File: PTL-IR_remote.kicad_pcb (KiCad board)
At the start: 2 copper layers, 25.4 x 40.1 mm, 22 parts, among them J1 8p, J2 8p, J3 bme280, J4 Conn_01x03_Female, Q1 2N7002, U1 TSOP4838

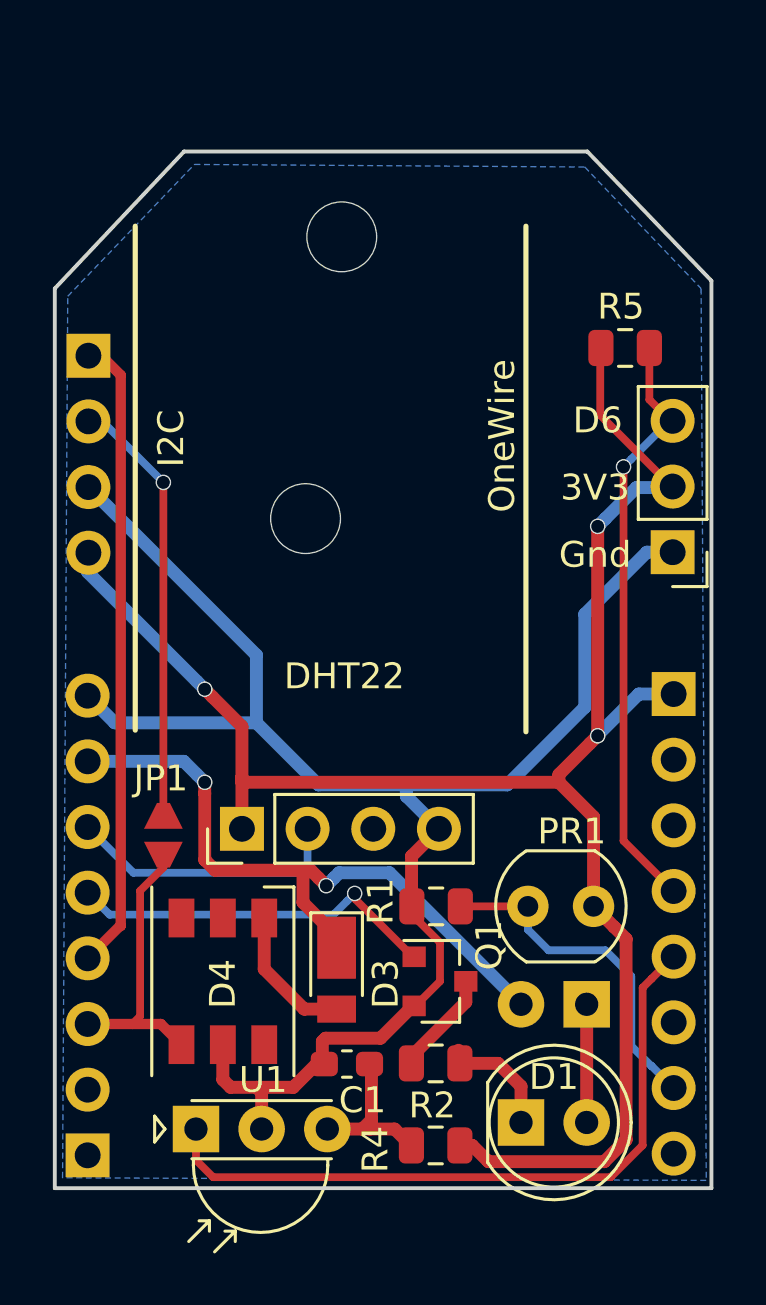
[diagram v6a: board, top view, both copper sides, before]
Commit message: Moved to Kicad5 Fixed swap of 5V and GND PCB is now V1.2
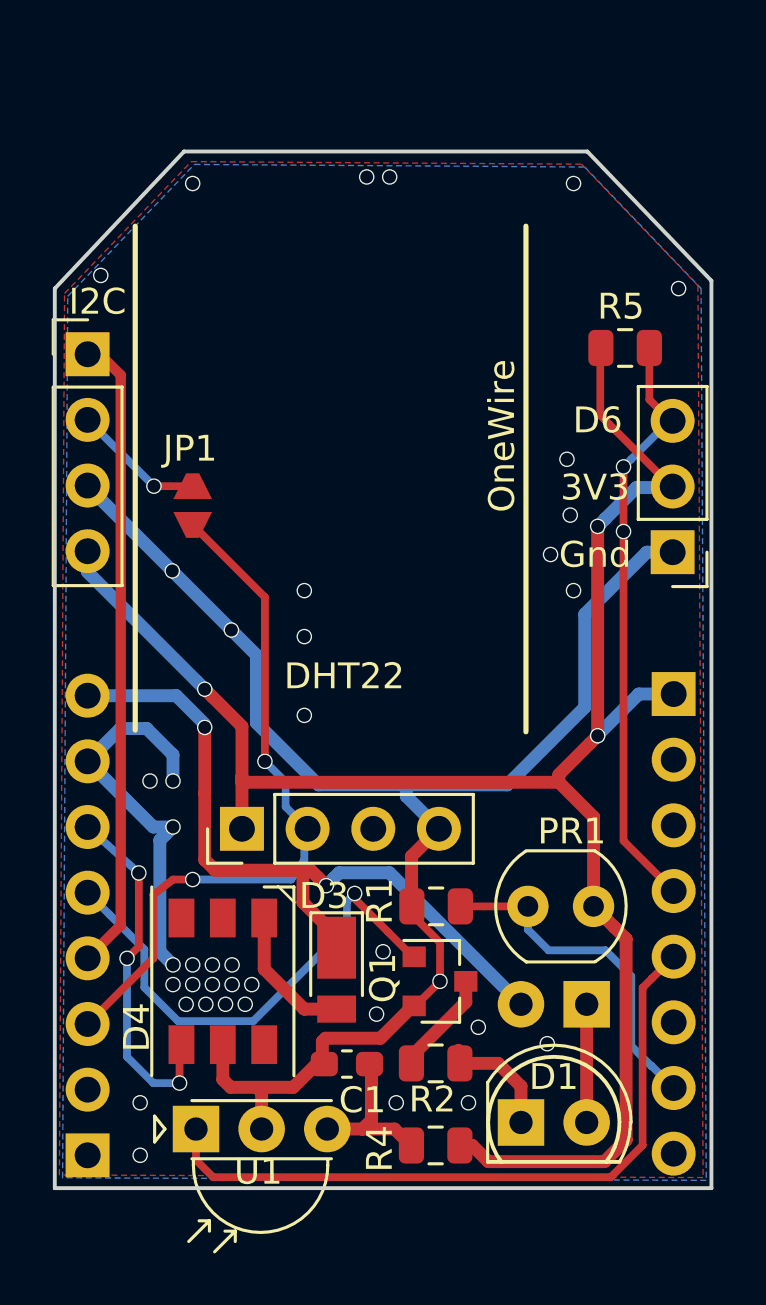
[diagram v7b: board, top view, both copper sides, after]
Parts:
- removed ?: , PTL-ino:PTL_mini
- removed G***: LOGO, PTL-ino:Logo_silk_CC-BY-SA_10x4.5mm
- removed J3: bme280, Connector_PinHeader_2.54mm:PinHeader_1x04_P2.54mm_Vertical
- removed bscrew, dscrew: MountingHole_2.7mm_M2.5, MountingHole:MountingHole_2.7mm_M2.5
- added bme280: bme280, Connector_PinHeader_2.54mm:PinHeader_1x04_P2.54mm_Vertical, F.Cu at (174.0, 87.1)
- moved JP1 12.8 mm to (178.1, 93.0)
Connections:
- D4 pad 2: (no net) -> Net-(D4-Pad2)
- D4 pad 3: (no net) -> Net-(D4-Pad3)
- D4 pad 4: D2 -> RGB
- D4 pad 6: (no net) -> Net-(D4-Pad6)
- J1 pad 2: (no net) -> Net-(J1-Pad2)
- J1 pad 3: (no net) -> Net-(J1-Pad3)
- J1 pad 6: (no net) -> Net-(J1-Pad6)
- J1 pad 8: (no net) -> Net-(J1-Pad8)
- J2 pad 1: (no net) -> Net-(J2-Pad1)
- J2 pad 2: (no net) -> Net-(J2-Pad2)
- J2 pad 3: D2 -> DHT
- J2 pad 6: DHT -> RGB
- J2 pad 7: +5V -> GNDREF
- J2 pad 8: GNDREF -> +5V
- JP1 pad 1: D2 -> DHT
- JP1 pad 2: /SCL -> Net-(JP1-Pad2)
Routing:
- net /SCL: track 17.4 -> 0.00 mm, vias 1 -> 0
- net DHT: track 11.4 -> 27.7 mm, vias 0 -> 2
- net RGB: track 0.00 -> 14.2 mm, vias 0 -> 3
- net D2: track 11.1 -> 0.00 mm
- net GNDREF: track 64.5 -> 72.9 mm, vias 0 -> 40
- net Net-(JP1-Pad2): track 0.00 -> 6.24 mm, vias 0 -> 1
- net IR: track 14.5 -> 19.3 mm
- net +5V: track 26.4 -> 28.6 mm
- net OneW: vias 1 -> 2
- added copper zone on F.Cu, net GNDREF
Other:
- rule trace_min: 0.2 -> 0.3
- board text added: "v1.2"
- board text removed: "v1.1"

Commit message: forgot to add some modified files
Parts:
- added ?: MountingHole_2.7mm_M2.5, MountingHole:MountingHole_2.7mm_M2.5, F.Cu at (183.9, 82.5)
- added ?: MountingHole_2.7mm_M2.5, MountingHole:MountingHole_2.7mm_M2.5, F.Cu at (181.9, 93.2)
- added ?: , PTL-ino:PTL_mini, B.Cu at (192.5, 93.2)
- added G***: LOGO, PTL-ino:Logo_silk_CC-BY-SA_10x4.5mm, B.Cu at (182.1, 113.3)
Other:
- board text added: "v1.3"
- board text removed: "v1.2"
